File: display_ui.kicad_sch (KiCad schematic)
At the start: 74 parts, among them SW401 K2-1102SP-C4SC-04, SW402 K2-1102SP-C4SC-04, SW403 K2-1102SP-C4SC-04, SW404 K2-1102SP-C4SC-04, SW405 PEC11R-4220F-S0012, T401 AO3400A, T402 AO3400A, T403 AO3400A, T404 AO3400A, T405 AO3400A, T406 AO3400A, X401 ER-TFT035-6

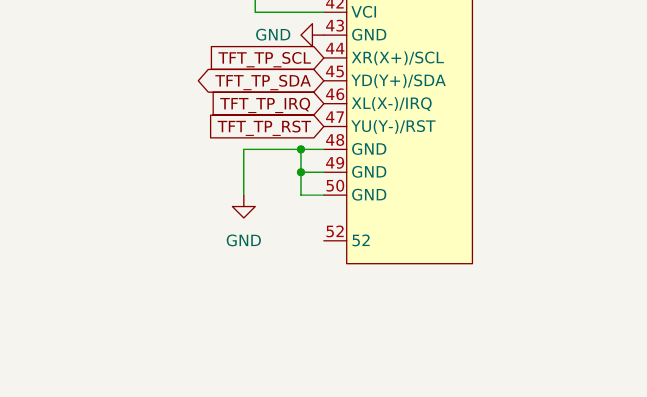
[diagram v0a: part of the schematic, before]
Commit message: add tft touch controller info, work on mpcie pinout
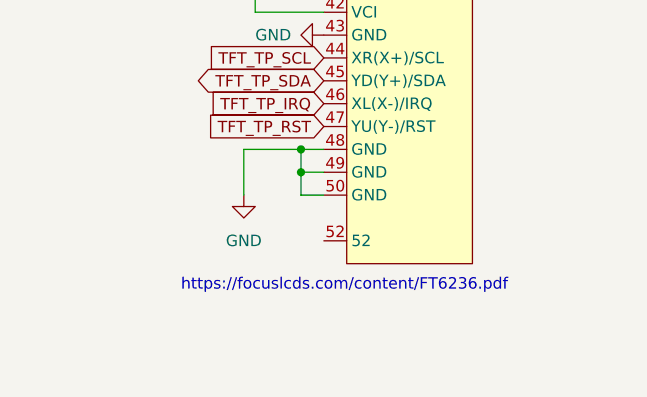
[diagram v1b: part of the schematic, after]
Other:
- note added: "https://focuslcds.com/content/FT6236.pdf"
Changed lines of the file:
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@@
+    (effects (font (size 1.27 1.27)) (justify left bottom))
+  )
+  (text "https://focuslcds.com/content/FT6236.pdf" (at 233.045 164.465 0)
     (effects (font (size 1.27 1.27)) (justify left bottom))
   )

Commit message: start rework of baseboard.
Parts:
- renumbered BUZZER401 to BUZZER1, C401 to C17, C402 to C18, C403 to C19, C404 to C20, C405 to C21, C406 to C22, C407 to C23, C408 to C24, C409 to C25, C410 to C26, C411 to C27, D405 to D10, D406 to D11, D407 to D12, D408 to D13, D409 to D14, D410 to D15, D411 to D16, D401 to D6, D402 to D7, D403 to D8, D404 to D9, R401 to R10, R402 to R11, R403 to R12, R404 to R13, R405 to R14, R406 to R15, R407 to R16, R408 to R17, R409 to R18, R410 to R19, R411 to R20, R412 to R21, R413 to R22, R414 to R23, R415 to R24, R416 to R25, R417 to R26, R418 to R27, R419 to R28, R420 to R29, R421 to R30, R422 to R31, R423 to R32, R424 to R33, R425 to R34, R426 to R35, R427 to R36, R428 to R37, R429 to R38, R430 to R39, R431 to R40, R432 to R41, R433 to R42, R434 to R43, R435 to R44, R436 to R45, R437 to R46, R438 to R47, R439 to R48, SW401 to SW2, SW402 to SW3, SW403 to SW4, SW404 to SW5, SW405 to SW6, T401 to T1, T402 to T2, T403 to T3, T404 to T4, T405 to T5, T406 to T6, X401 to X6

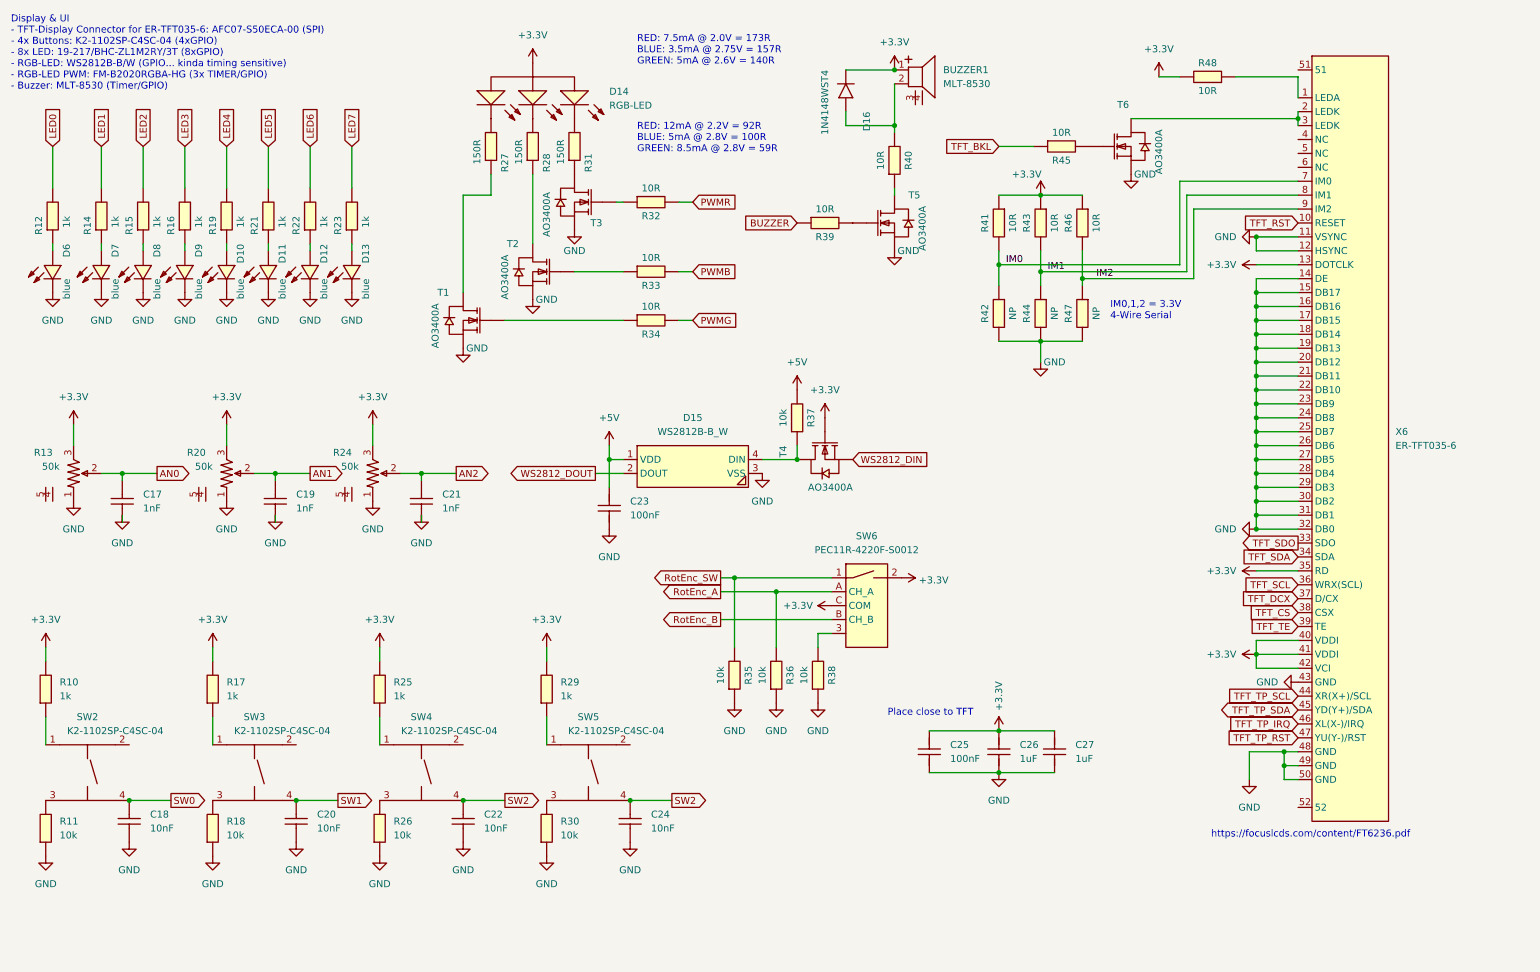
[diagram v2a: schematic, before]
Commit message: rework schematic. remove unnescessary stuff. Connect PCIE Connector. Select new Temperature Sensor (I2C) Define Signals for 40Pin Connector
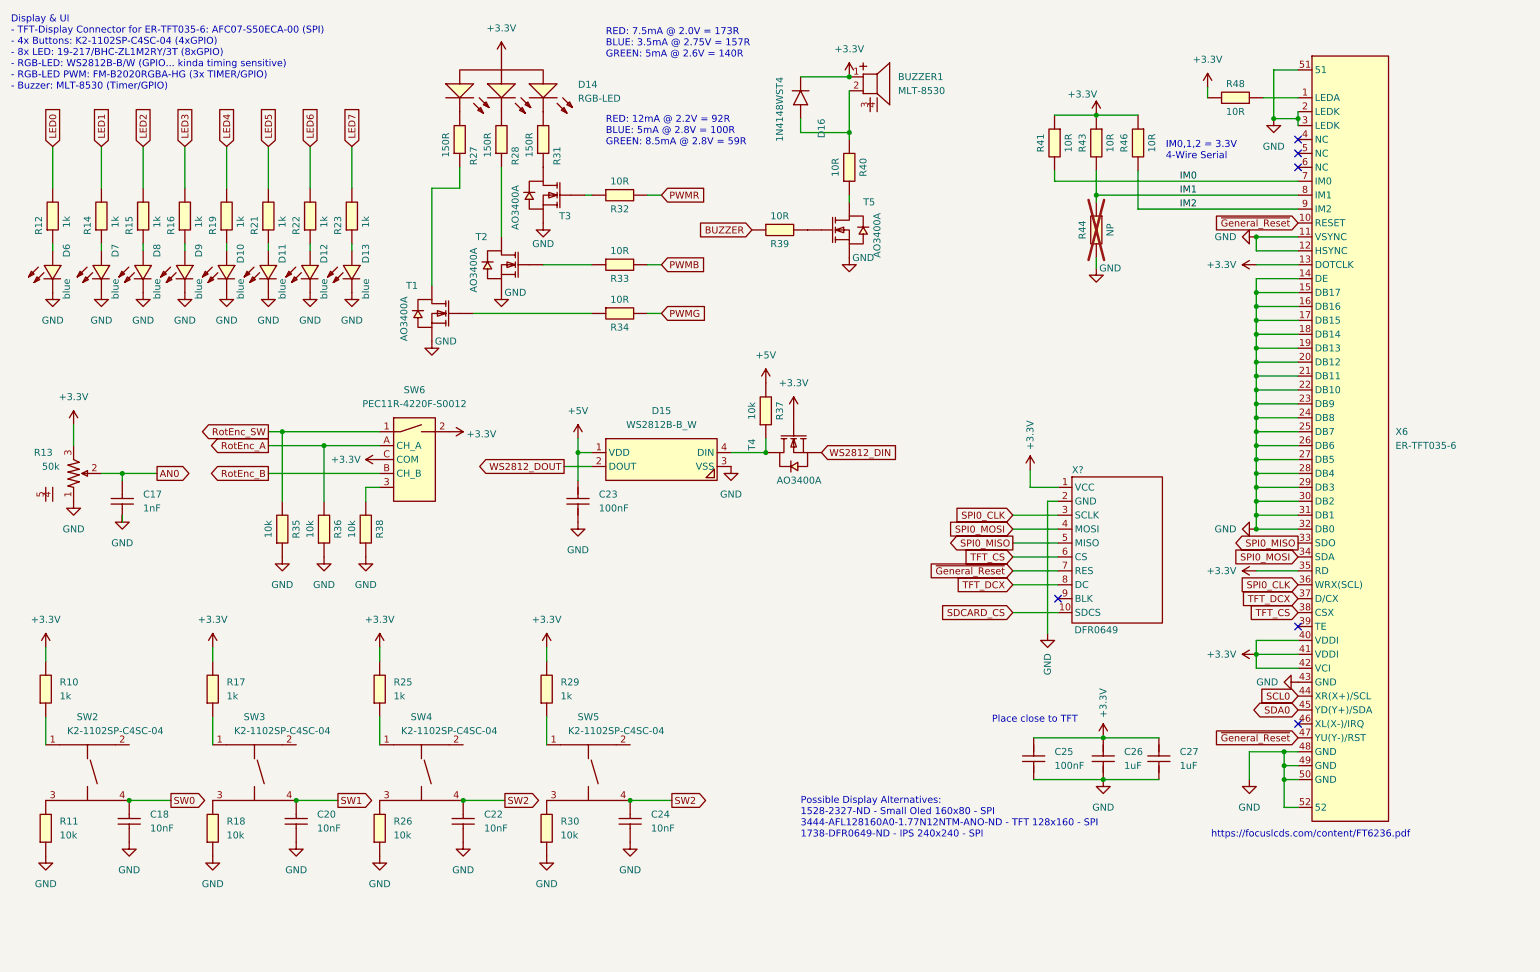
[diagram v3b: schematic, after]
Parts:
- removed C19, C21: 1nF, eduboardv2:C0402, symbol eduboardv2:0402B102K500NT
- removed R20, R24: 50k, eduboardv2:RES-TH_RK09K1130AAU, symbol eduboardv2:RK09K1130ACL
- removed R42, R47: NP, eduboardv2:R0402, symbol eduboardv2:0402WGF100JTCE
- removed R45: 10R, eduboardv2:R0402, symbol eduboardv2:0402WGF100JTCE
- removed T6: AO3400A, eduboardv2:SOT-23-3_L2.9-W1.6-P1.90-LS2.8-BR, symbol eduboardv2:AO3400A
- added X?: DFR0649, EduboardV2_kicadlib:DFR0649, symbol EduboardV2_kicadlib:DFR0649
- R44: now not fitted
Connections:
- net TFT_TP_RST is gone; now on net ~{General_Reset}: X6.47 (YU(Y-)/RST)
- net +3.3V: now also X?.1 (VCC)
- net GND: now also X6.2 (LEDK), X6.3 (LEDK), X6.51, X6.52, X?.2 (GND)
- net TFT_CS: now also X?.6 (CS)
- net TFT_DCX: now also X?.8 (DC)
- net TFT_RST renamed ~{General_Reset}
- net ~{General_Reset}: now also X?.7 (RES)
- net TFT_SCL renamed SPI0_CLK
- net SPI0_CLK: now also X?.3 (SCLK)
- net TFT_SDA renamed SPI0_MOSI
- net SPI0_MOSI: now also X?.4 (MOSI)
- net TFT_SDO renamed SPI0_MISO
- net SPI0_MISO: now also X?.5 (MISO)
- net TFT_TE: no longer names the net of X6.39 (TE)
- net TFT_TP_IRQ: no longer names the net of X6.46 (XL(X-)/IRQ)
- net TFT_TP_SCL renamed SCL0
- net TFT_TP_SDA renamed SDA0
- new net SDCARD_CS: X?.10 (SDCS)
- no-connect marks 0 -> 6
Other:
- note added: "Possible Display Alternatives: 1528-2327-ND - Small Oled 160x80 - SPI 3444-AFL128160A0-1.77N12NTM-ANO-ND - TFT 128x160 - SPI 1738-DFR0649-ND - IPS 240x240 - SPI"
- moved on the sheet: BUZZER1, C23, C25, C26, C27, D14, D15, D16, R27, R28, R31, R32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

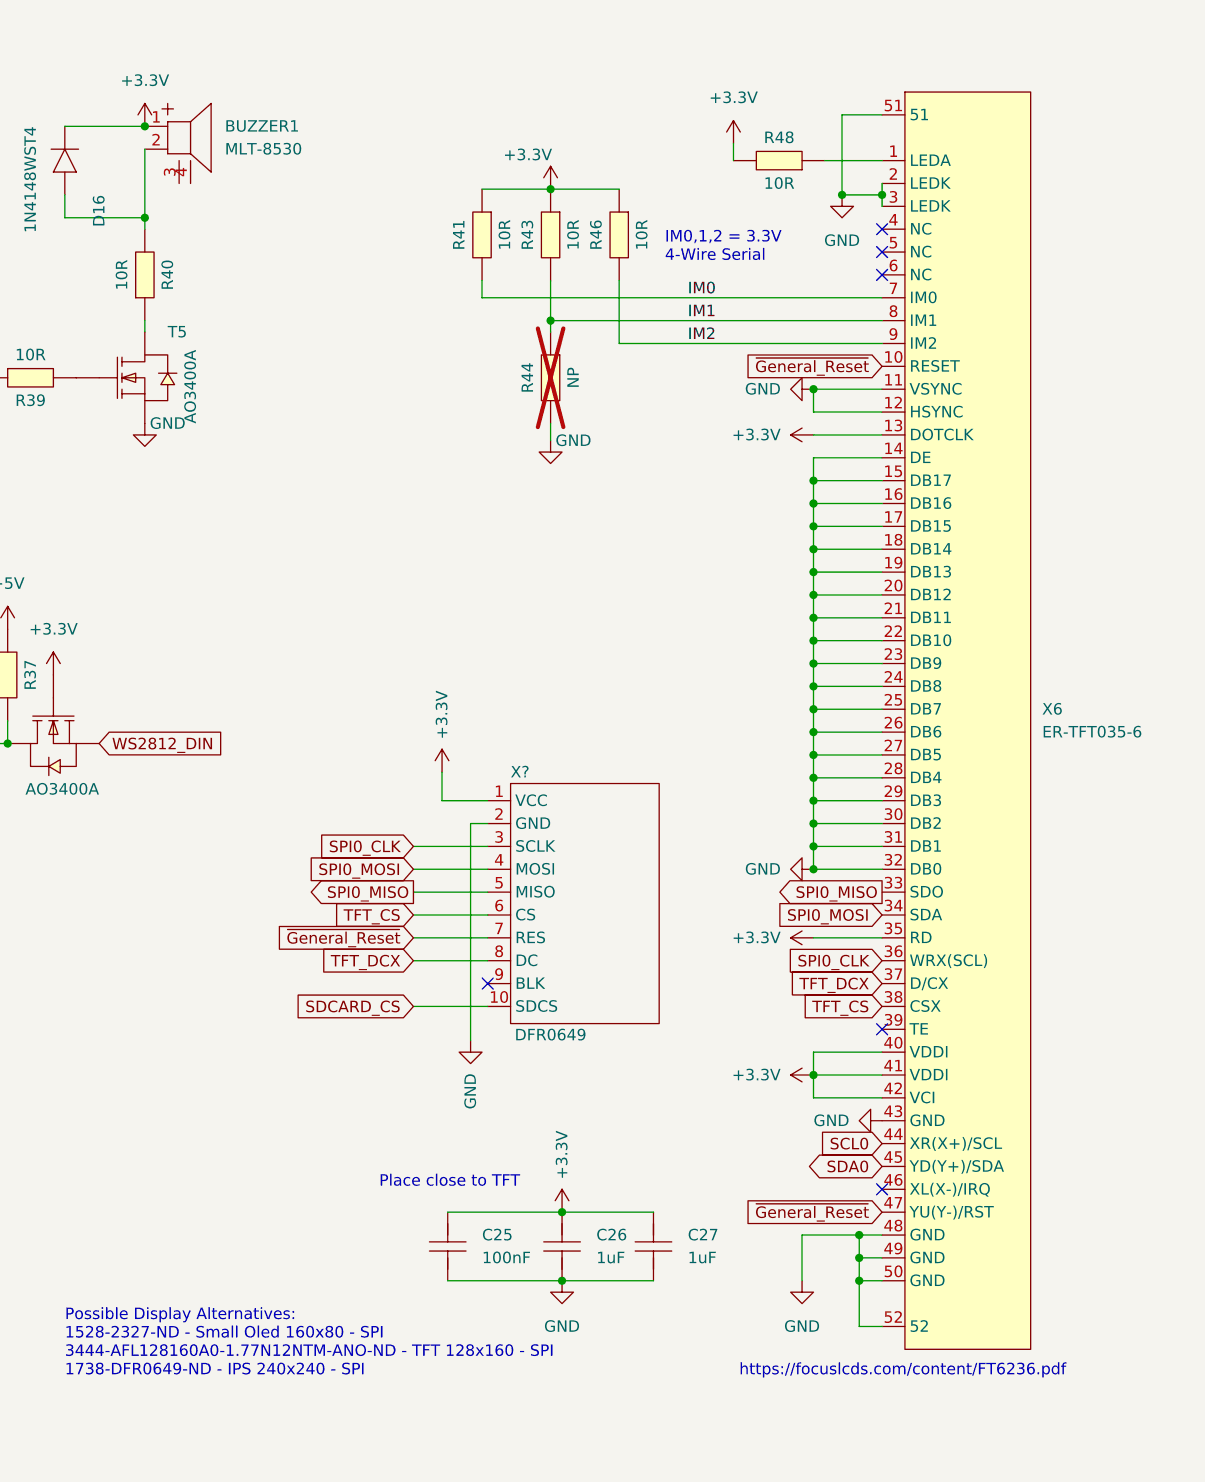
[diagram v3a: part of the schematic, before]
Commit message: replace display with better module, start layout parts on pcb.
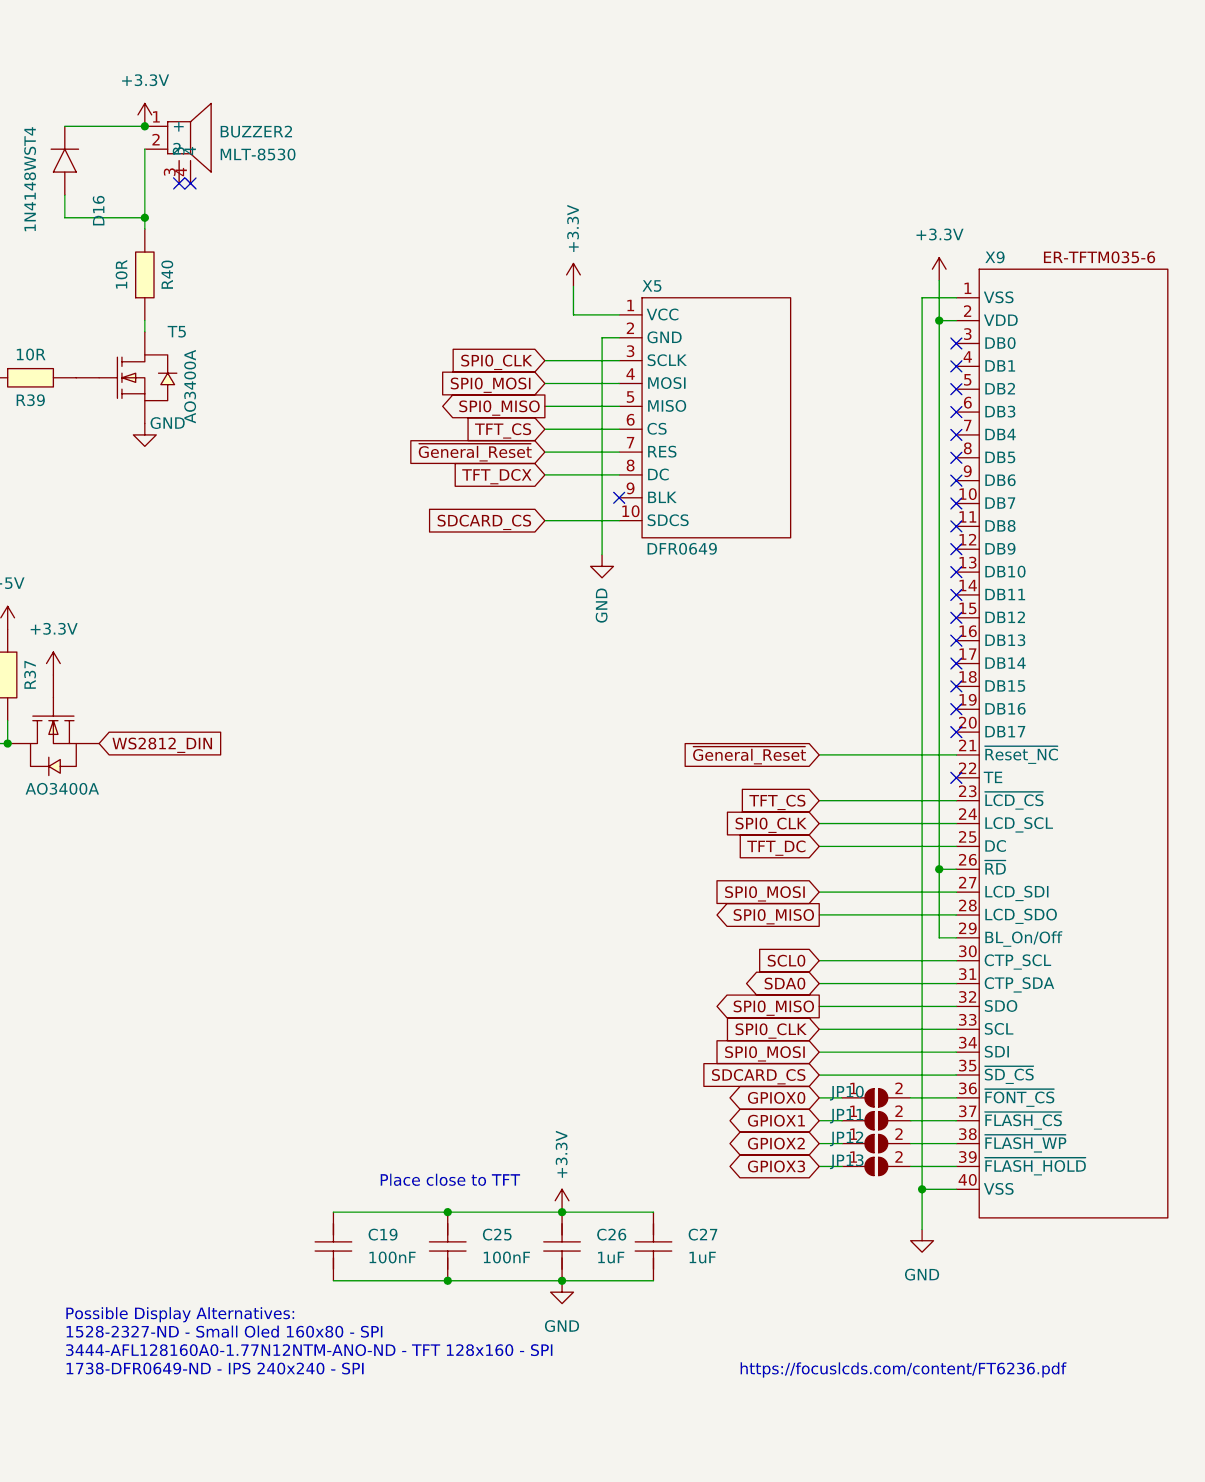
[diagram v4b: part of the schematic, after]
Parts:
- removed BUZZER1: MLT-8530, eduboardv2:BUZ-SMD_4P-L8.5-W8.5-P8.50-TL, symbol eduboardv2:MLT-8530
- removed R41, R43, R46, R48: 10R, eduboardv2:R0402, symbol eduboardv2:0402WGF100JTCE
- removed R44: NP, eduboardv2:R0402, symbol eduboardv2:0402WGF100JTCE
- removed X6: ER-TFT035-6, eduboardv2:FPC-SMD_AFC07-S50ECA-00, symbol eduboardv2:ER-TFT035-6
- added BUZZER2: MLT-8530, EduboardV2_kicadlib:BUZ-SMD_4P-L8.5-W8.5-P8.50-BR, symbol EduboardV2_kicadlib:MLT-8530
- added C19: 100nF, Capacitor_SMD:C_0402_1005Metric_Pad0.74x0.62mm_HandSolder, symbol eduboardv2:CL05B104KB54PNC
- added JP10, JP11, JP12, JP13: SolderJumper_2_Open, symbol Jumper:SolderJumper_2_Open
- added X9: ~, EduboardV2_kicadlib:HDR-SMD_40P-P2.54-V-F-R2-C20-S7.1-EH, symbol EduboardV2_kicadlib:ER-TFTM035-6
- C17, C18, C20, C22, C23, C24, C25, C26, C27: footprint eduboardv2:C0402 -> Capacitor_SMD:C_0402_1005Metric_Pad0.74x0.62mm_HandSolder
- D10, D11, D12, D13, D6, D7, D8, D9: footprint eduboardv2:LED0603-R-RD_BLUE -> EduboardV2_kicadlib:LED0603-FD_BLUE
- D14: footprint eduboardv2:LED-SMD_FM-B2020RGBA-HG -> EduboardV2_kicadlib:LED-SMD_FM-B2020RGBA-HG
- D15: footprint eduboardv2:LED-SMD_4P-L5.0-W5.0-TL_WS2812B-B -> EduboardV2_kicadlib:LED-SMD_4P-L5.0-W5.0-TL_WS2812B-B
- D16: footprint eduboardv2:SOD-323_L1.8-W1.3-LS2.5-RD -> EduboardV2_kicadlib:SOD-323_L1.8-W1.3-LS2.5-RD
- R10, R11, R12, R14, R15, R16, R17, R18, R19, R21, R22, R23, R25, R26, R27, R28, R29, R30, R31, R32, R33, R34, R35, R36, R37, R38, R39, R40: footprint eduboardv2:R0402 -> Resistor_SMD:R_0402_1005Metric_Pad0.72x0.64mm_HandSolder
- R13: footprint eduboardv2:RES-TH_RK09K1130AAU -> EduboardV2_kicadlib:RES-TH_RK09K1130AAU
- SW2, SW3, SW4, SW5: footprint eduboardv2:KEY-SMD_4P-L6.0-W6.0-P4.50-LS9.5-BL -> EduboardV2_kicadlib:KEY-SMD_4P-L6.0-W6.0-P4.50-LS9.5-BL
- SW6: footprint SW-TH_PEC11R-4220F-S0012 -> EduboardV2_kicadlib:SW-TH_PEC11R-4220F-S0012
- T1, T2, T3, T4, T5: footprint eduboardv2:SOT-23-3_L2.9-W1.6-P1.90-LS2.8-BR -> EduboardV2_kicadlib:SOT-23-3_L2.9-W1.6-P1.90-LS2.8-BR
- gave numbers to parts that had none: 1
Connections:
- net +3.3V: now also BUZZER2.1 (+), C19.2, X9.2 (VDD), X9.26 (~{RD}), X9.29 (BL_On/Off)
- net GND: now also C19.1, X9.1 (VSS), X9.40 (VSS)
- net SCL0: now also X9.30 (CTP_SCL)
- net SDA0: now also X9.31 (CTP_SDA)
- net SDCARD_CS: now also X9.35 (~{SD_CS})
- net SPI0_CLK: now also X9.24 (LCD_SCL), X9.33 (SCL)
- net SPI0_MISO: now also X9.28 (LCD_SDO), X9.32 (SDO)
- net SPI0_MOSI: now also X9.27 (LCD_SDI), X9.34 (SDI)
- net TFT_CS: now also X9.23 (~{LCD_CS})
- net ~{General_Reset}: now also X9.21 (~{Reset_NC})
- net at D16.2 (A), R40.2: now also BUZZER2.2
- new net: JP13.2 (B), X9.39 (~{FLASH_HOLD})
- new net: JP12.2 (B), X9.38 (~{FLASH_WP})
- new net: JP11.2 (B), X9.37 (~{FLASH_CS})
- new net: JP10.2 (B), X9.36 (~{FONT_CS})
- new net GPIOX0: JP10.1 (A)
- new net GPIOX1: JP11.1 (A)
- new net GPIOX2: JP12.1 (A)
- new net GPIOX3: JP13.1 (A)
- new net TFT_DC: X9.25 (DC)
- no-connect marks 6 -> 22
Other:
- note removed: "IM0,1,2 = 3.3V 4-Wire Serial"
- moved on the sheet: X5

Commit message: Layout of parts done. Started laying tracks
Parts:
- removed SW2, SW3, SW4, SW5: K2-1102SP-C4SC-04, EduboardV2_kicadlib:KEY-SMD_4P-L6.0-W6.0-P4.50-LS9.5-BL, symbol eduboardv2:K2-1102SP-C4SC-04
- added SW2, SW3, SW4, SW5: K2-1102SP-C4SC-04, EduboardV2_kicadlib:KEY-SMD_4P-L6.0-W6.0-P4.50-LS9.5-BL, symbol EduboardV2_kicadlib:K2-1102SP-C4SC-04
- JP10, JP11, JP12, JP13: footprint (none) -> Jumper:SolderJumper-2_P1.3mm_Open_Pad1.0x1.5mm
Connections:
- net RotEnc_B: now also R38.2
- net SW0: now also R11.2, SW2.3, SW2.4
- net SW1: now also R18.2, SW3.3, SW3.4
- net SW2: now also R26.2, R30.2, SW4.3, SW4.4, SW5.3, SW5.4
- net at SW6.3: no longer R38.2
- net at R10.1: now also SW2.1, SW2.2
- net at R17.1: now also SW3.1, SW3.2
- net at R29.1: now also SW5.1, SW5.2
- net at R25.1: now also SW4.1, SW4.2
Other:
- moved on the sheet: C18, C20, C22, C24, R11, R18, R26, R30

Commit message: proceed with layout
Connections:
- net TFT_DCX is gone; now on net TFT_DC: X5.8 (DC)
- net GND: now also SW6.3
- net SW2: no longer C24.2, R30.2, SW5.3, SW5.4
- new net SW3: C24.2, R30.2, SW5.3, SW5.4
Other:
- moved on the sheet: R35, R36, R38
